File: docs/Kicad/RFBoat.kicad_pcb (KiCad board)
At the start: 2 copper layers, 38.9 x 64.8 mm, 13 parts, among them SW1 SW_DPST, U1 L293D, U2 5V regulator, U3 NRF24L01_Breakout

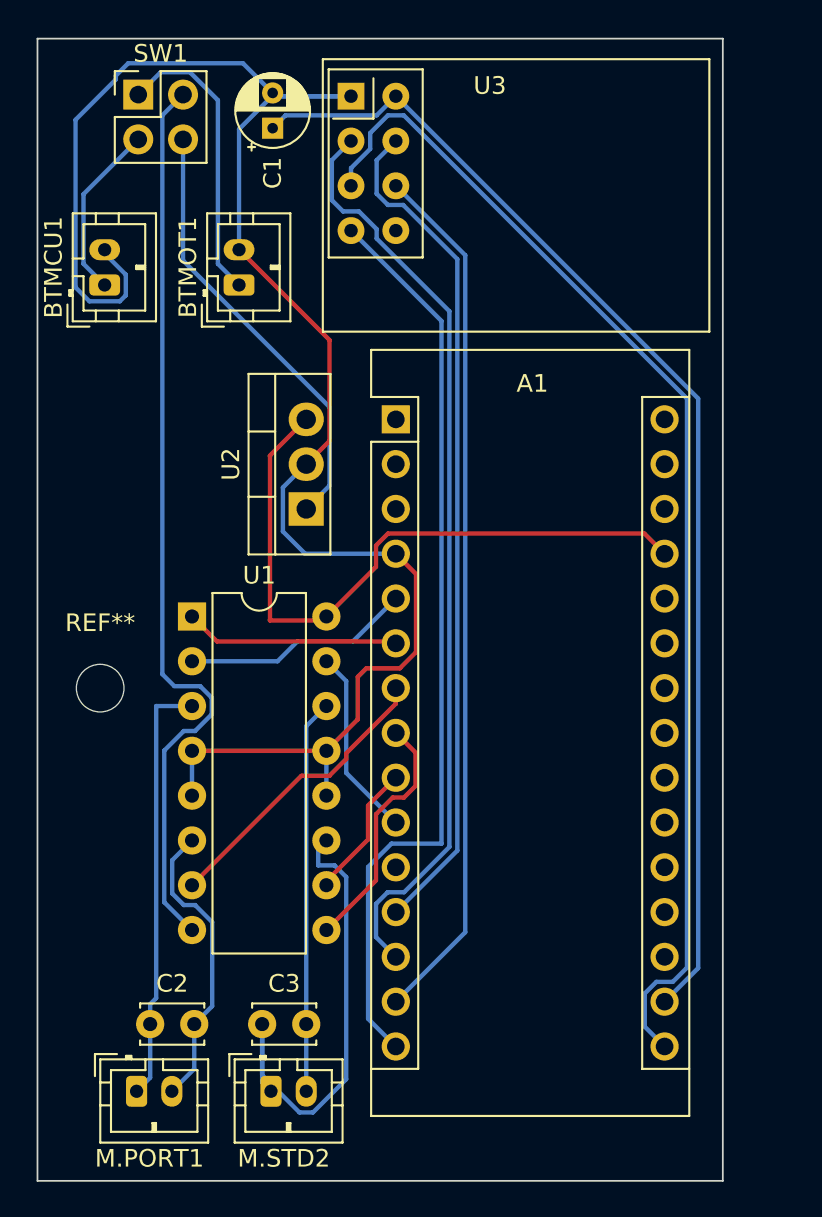
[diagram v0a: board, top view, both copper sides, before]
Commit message: changed pin layout to free last PWM pin (10) CE & CSN
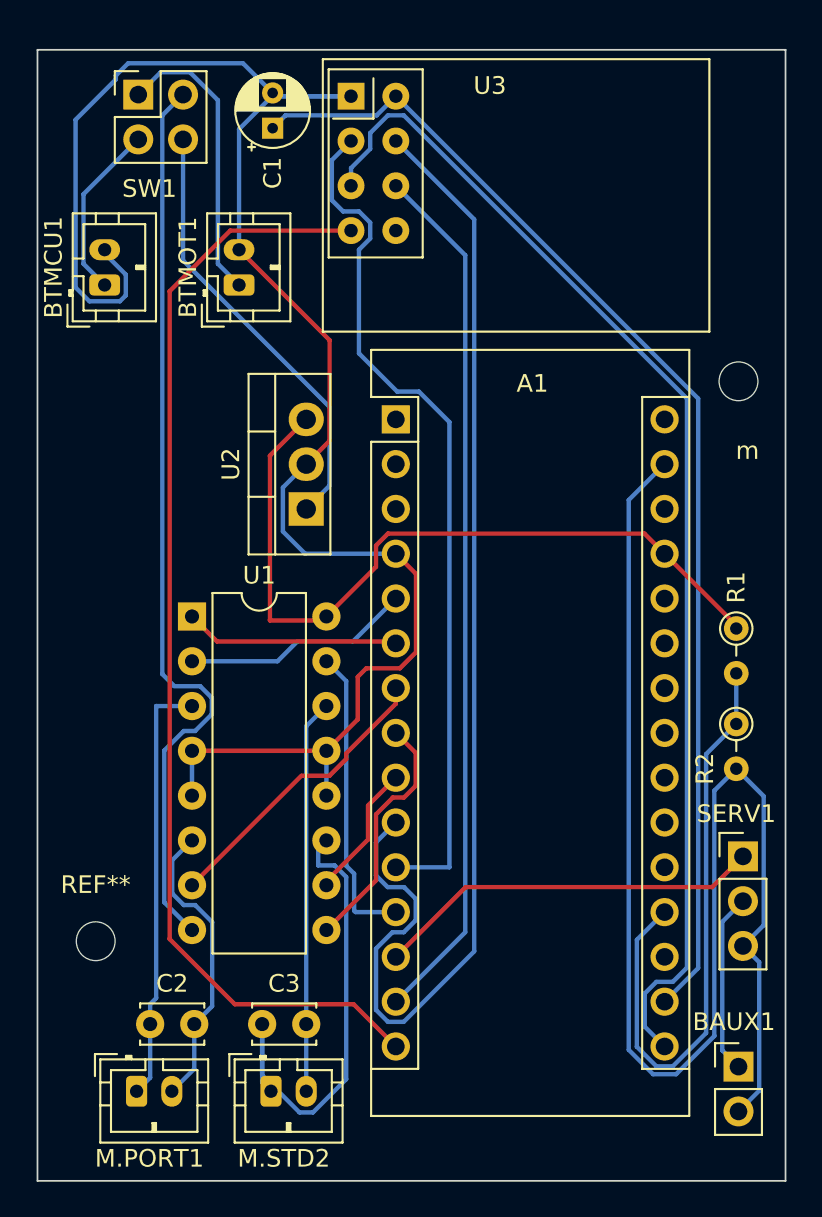
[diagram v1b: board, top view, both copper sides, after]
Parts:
- removed the REF** at (105.2, 86.4)
- added BAUX1: Battery, Connector_PinHeader_2.54mm:PinHeader_1x02_P2.54mm_Vertical, F.Cu at (141.4, 107.8)
- added R1: R_Photo, Resistor_THT:R_Axial_DIN0204_L3.6mm_D1.6mm_P2.54mm_Vertical, F.Cu at (141.2, 83.0)
- added R2: R, Resistor_THT:R_Axial_DIN0204_L3.6mm_D1.6mm_P2.54mm_Vertical, F.Cu at (141.2, 88.4)
- added REF**: MountingHole_2.2mm_M2, MountingHole:MountingHole_2.2mm_M2, F.Cu at (104.9, 100.7)
- added SERV1: Motor_Servo, Connector_PinHeader_2.54mm:PinHeader_1x03_P2.54mm_Vertical, F.Cu at (141.6, 95.9)
- added m: MountingHole_2.2mm_M2, MountingHole:MountingHole_2.2mm_M2, F.Cu at (141.4, 69.0)
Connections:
- A1 pad 10: Net-(A1-Pad10) -> Net-(U3-Pad4)
- A1 pad 11: unconnected-(A1-Pad11) -> Net-(U3-Pad3)
- A1 pad 19: unconnected-(A1-Pad19) -> Net-(A1-Pad19)
- A1 pad 29: unconnected-(A1-Pad29) -> Net-(A1-Pad29)
- U1 pad 15: Net-(A1-Pad10) -> Net-(A1-Pad12)
- U3 pad 3: Net-(A1-Pad13) -> Net-(U3-Pad3)
- U3 pad 4: Net-(A1-Pad12) -> Net-(U3-Pad4)
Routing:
- net Net-(A1-Pad29): track 0.00 -> 77.5 mm
- net Net-(U3-Pad4): track 0.00 -> 69.2 mm
- net Net-(U3-Pad3): track 0.00 -> 49.2 mm
- net Net-(A1-Pad19): track 0.00 -> 34.6 mm
- net Net-(A1-Pad12): track 48.0 -> 17.2 mm
- net Net-(A1-Pad13): track 52.7 -> 22.0 mm
- net Net-(A1-Pad15): track 52.4 -> 63.8 mm
- net Net-(A1-Pad10): track 10.8 -> 0.00 mm
- net Net-(BAUX1-Pad1): track 0.00 -> 10.3 mm
- net Net-(A1-Pad27): track 37.9 -> 43.8 mm
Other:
- board size 38.9 x 64.8 mm -> 42.4 x 64.1 mm
